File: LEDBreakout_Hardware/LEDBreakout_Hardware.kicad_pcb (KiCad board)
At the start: 2 copper layers, 39.9 x 39.9 mm, 29 parts, among them Q1 BSS138, Q2 BSS138, Q3 BSS138, Q4 BSS138

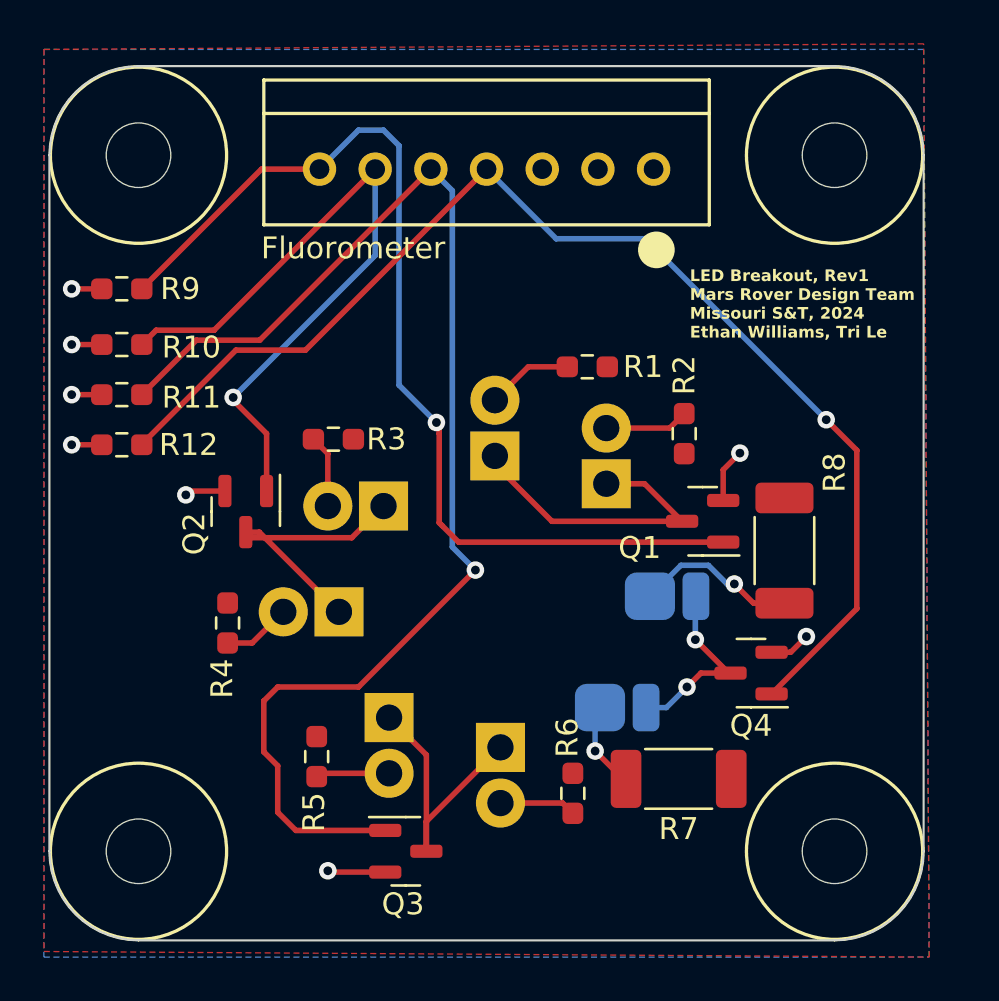
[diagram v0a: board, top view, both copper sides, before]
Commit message: Center diodes and regenerate Gerbs
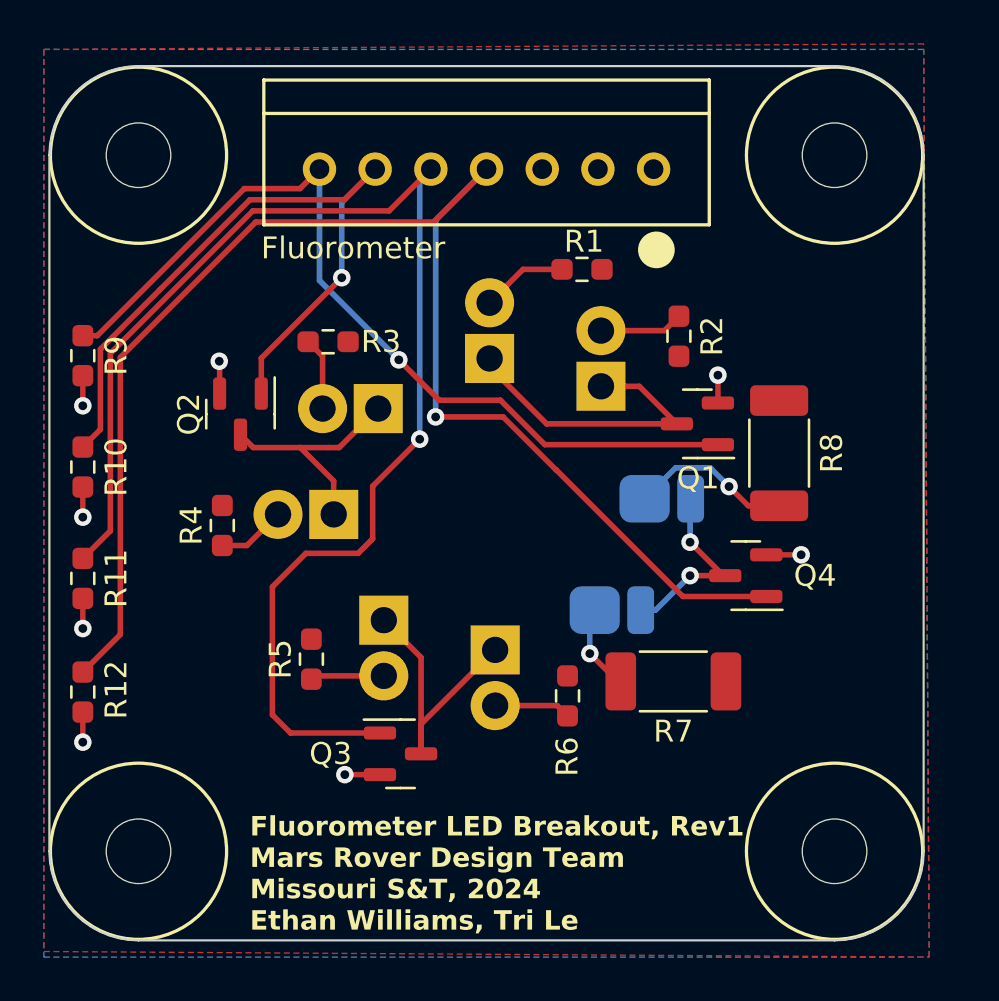
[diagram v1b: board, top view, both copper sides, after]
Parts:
- moved R12 11.4 mm to (66.0, 88.0), turned to -90 degrees
- moved R11 8.57 mm to (66.0, 82.8), turned to -90 degrees
- moved R10 5.86 mm to (66.0, 77.7), turned to -90 degrees
- moved D2 4.45 mm to (89.7, 74.0)
- moved D4 4.45 mm to (77.5, 79.9)
- moved D6 4.45 mm to (84.8, 86.1)
- moved D7 4.45 mm to (90.6, 84.2)
- moved D8 4.45 mm to (92.9, 79.1)
- moved R1 4.45 mm to (88.8, 68.7)
- moved R2 4.45 mm to (93.2, 71.8)
- moved R5 4.45 mm to (76.5, 86.5)
- moved R8 4.45 mm to (97.8, 77.1)
- moved D1 4.45 mm to (84.6, 72.8)
- moved D3 4.45 mm to (79.5, 75.1)
- moved D5 4.45 mm to (79.8, 84.7)
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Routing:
- net 400nm: track 56.1 -> 66.1 mm
- net 530nm: track 46.3 -> 40.3 mm
- net 465nm: track 59.3 -> 62.5 mm
- net GND: track 14.4 -> 11.4 mm
- net Net-(D3-K): track 12.7 -> 10.9 mm
- net 522nm: track 32.3 -> 33.1 mm
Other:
- board text added: "Fluorometer LED Breakout, Rev1 Mars Rover Design Team Missouri S&T, 2024 Ethan Williams, Tri Le"
- board text removed: "LED Breakout, Rev1 Mars Rover Design Team Missouri S&T, 2024 Ethan Williams, Tri Le"
